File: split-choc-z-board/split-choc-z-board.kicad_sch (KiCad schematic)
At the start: 76 parts, among them J1 USB4105-GF-A, J2 USB4105-GF-A, SW1 SW_SPST, SW10 SW_SPST, SW11 SW_SPST, SW12 SW_SPST, SW13 SW_SPST, SW14 SW_SPST, SW15 SW_SPST, SW16 SW_SPST, SW17 SW_SPST, SW18 SW_SPST, SW19 SW_SPST, SW2 SW_SPST, SW20 SW_SPST, SW21 SW_SPST, SW22 SW_SPST, SW3 SW_SPST, SW4 SW_SPST, SW5 SW_SPST, SW6 SW_SPST, SW7 SW_SPST, SW8 SW_SPST, SW9 SW_SPST, U1 USBLC6-2SC6, U2 RP2040, U3 NCP1117-3.3_SOT223, U4 W25Q128JVS, U5 USBLC6-2SC6, X1 ABM8-272-T3

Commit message: Placed all components properly! 😄
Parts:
- removed H1, H2: MountingHole_Pad_MP, TestPoint:TestPoint_Pad_2.0x2.0mm, symbol Mechanical:MountingHole_Pad_MP
- removed U1: USBLC6-2SC6, Package_TO_SOT_SMD:SOT-23-6, symbol Power_Protection:USBLC6-2SC6
- added C17: 100n, Capacitor_SMD:C_0402_1005Metric, symbol Device:C
- added D_CLK1, D_DATA1, GND1, GP24, GP25: TestPoint, TestPoint:TestPoint_Pad_D2.0mm, symbol Connector:TestPoint
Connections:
- net +3.3V is gone; now on net +3V3: C10.1, C11.1, C5.1, C6.1, C7.1, C8.1, C9.1
- net +3V3: no longer SW1.2 (B), SW10.2 (B), SW11.2 (B), SW12.2 (B), SW13.2 (B), SW14.2 (B), SW15.2 (B), SW16.2 (B), SW17.2 (B), SW18.2 (B), SW19.2 (B), SW2.2 (B), SW20.2 (B), SW3.2 (B), SW4.2 (B), SW5.2 (B), SW6.2 (B), SW7.2 (B), SW8.2 (B), SW9.2 (B), U2.3 (GPIO1), U2.4 (GPIO2), U2.5 (GPIO3), U2.6 (GPIO4)
- net B-B_D+: now also U5.1 (I/O1), U5.6 (I/O1)
- net B-B_D-: now also U5.3 (I/O2), U5.4 (I/O2)
- net DEBUG_CLK: now also D_CLK1.1
- net DEBUG_DATA: now also D_DATA1.1
- net GND: now also C17.1, GND1.1
- net RST: now also C17.2
- net USB_D+: no longer U5.1 (I/O1), U5.6 (I/O1)
- net USB_D-: no longer U5.3 (I/O2), U5.4 (I/O2)
- net GP24: now reaches U2.36 (GPIO24)
- net GP24: now also GP24.1
- net GP25: now reaches U2.37 (GPIO25)
- net GP25: now also GP25.1
- new net Col_1: SW1.2 (B), SW13.2 (B), SW17.2 (B), SW5.2 (B), SW9.2 (B), U2.3 (GPIO1)
- new net Col_2: SW10.2 (B), SW14.2 (B), SW18.2 (B), SW2.2 (B), SW6.2 (B), U2.4 (GPIO2)
- new net Col_3: SW11.2 (B), SW15.2 (B), SW19.2 (B), SW3.2 (B), SW7.2 (B), U2.5 (GPIO3)
- new net Col_4: SW12.2 (B), SW16.2 (B), SW20.2 (B), SW4.2 (B), SW8.2 (B), U2.6 (GPIO4)
- no-connect marks 24 -> 22
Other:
- note removed: "ESD Protection"
- moved on the sheet: R8, SW22

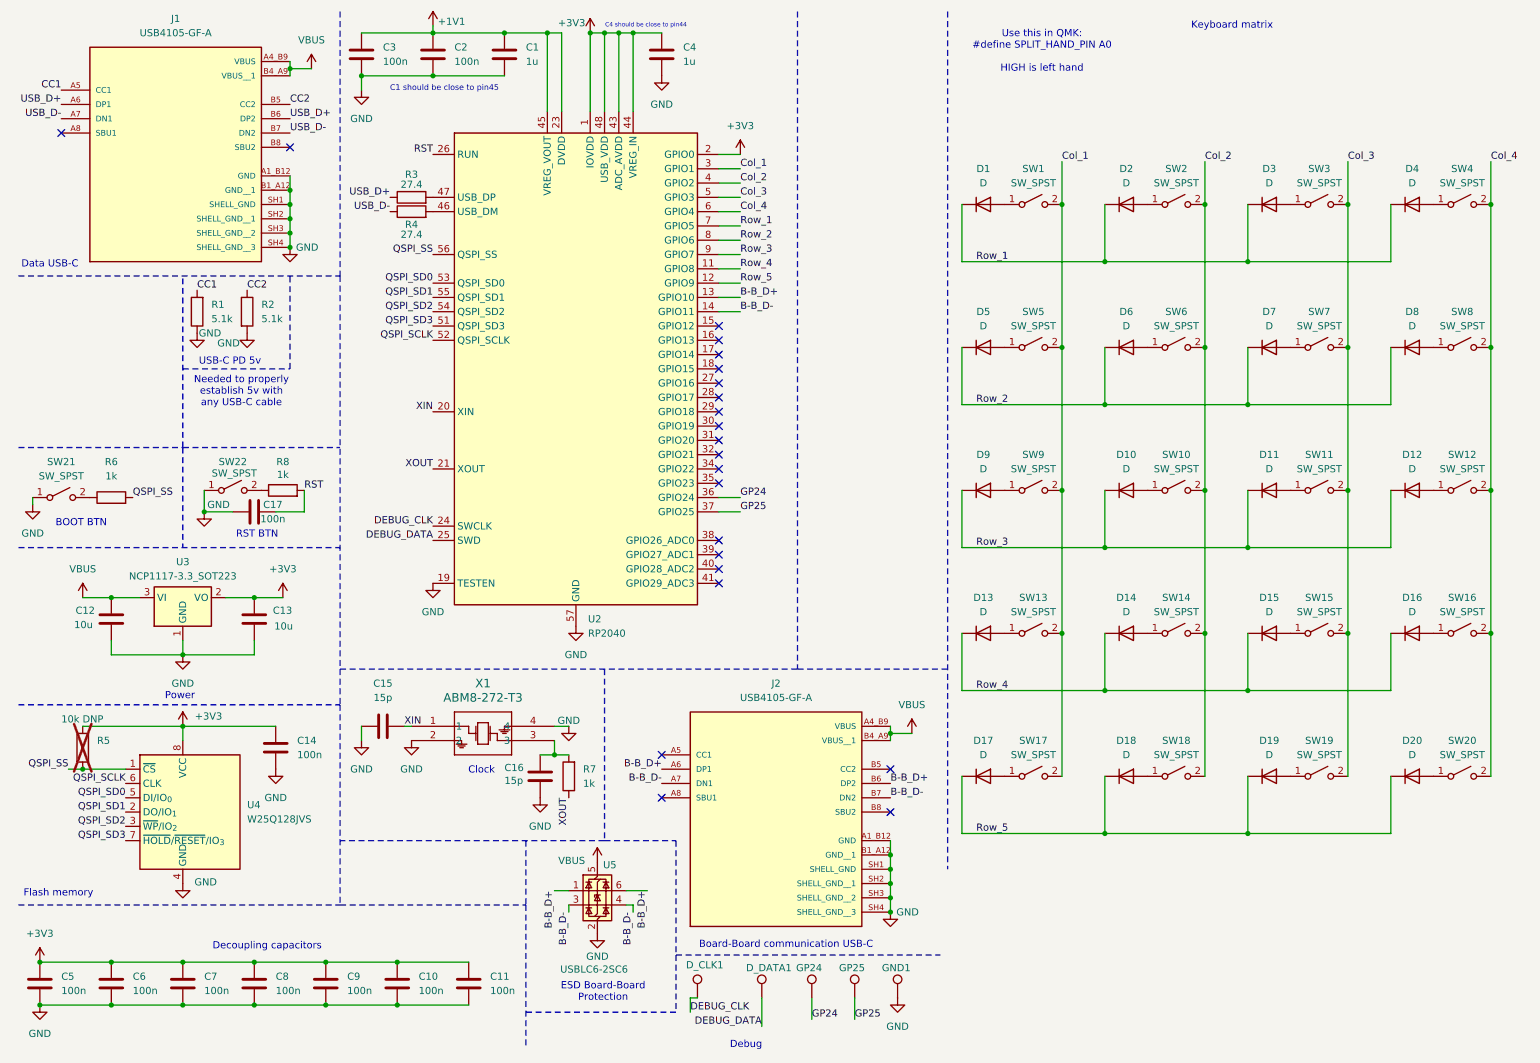
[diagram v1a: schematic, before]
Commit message: Routed left side
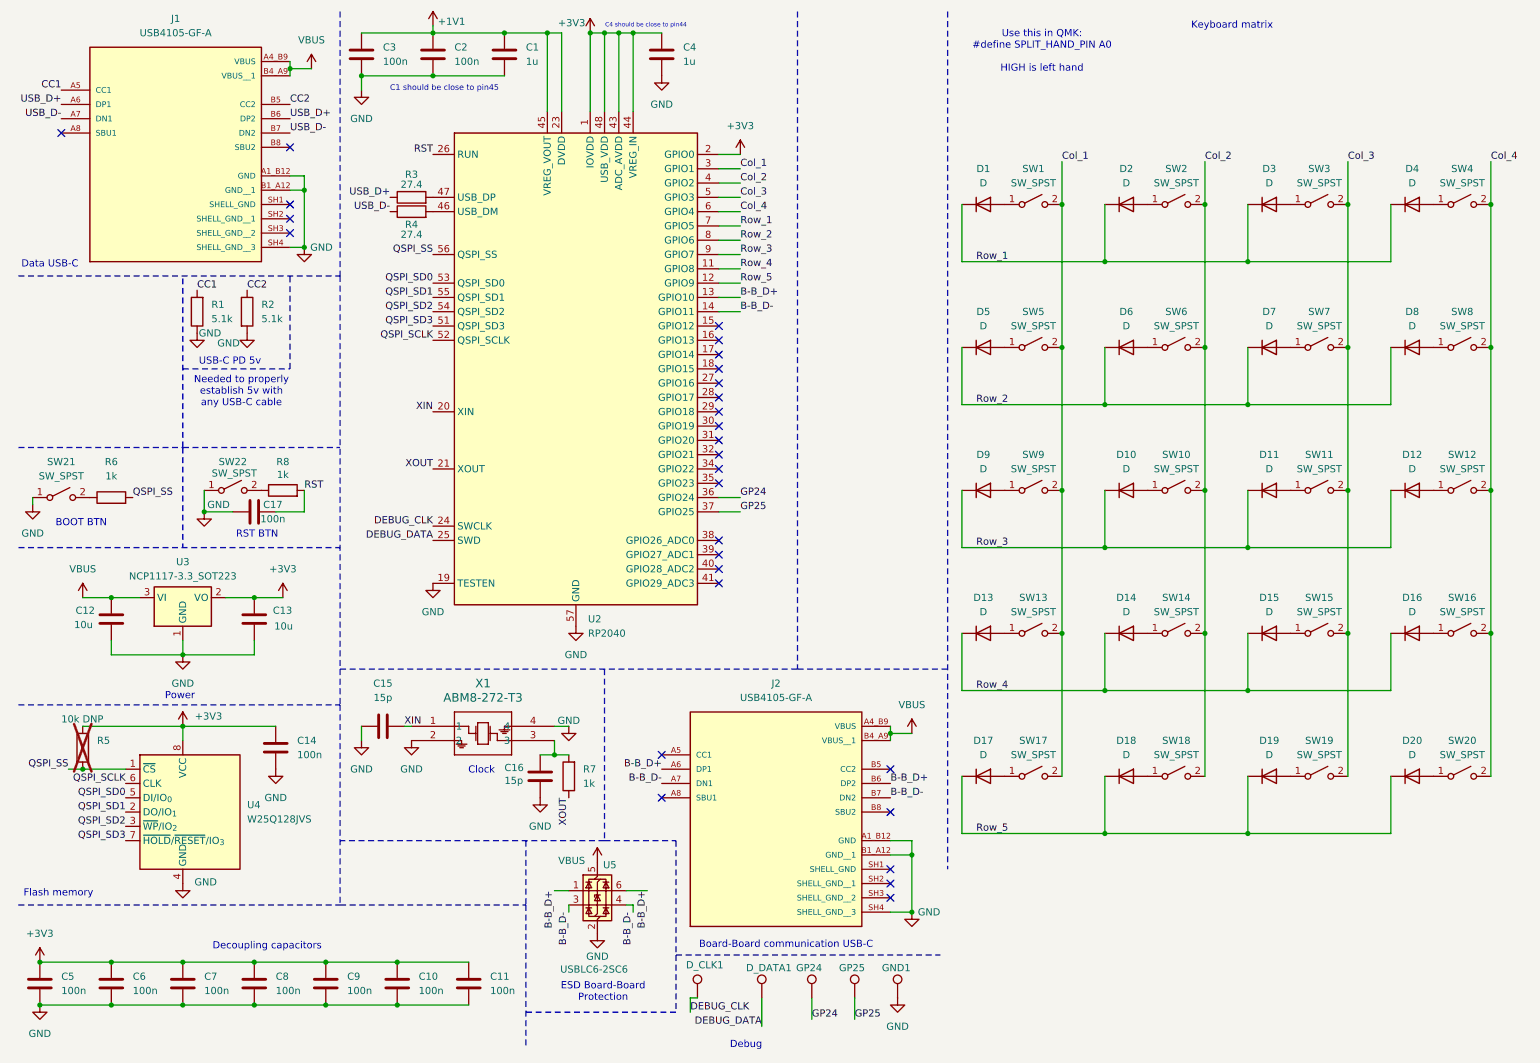
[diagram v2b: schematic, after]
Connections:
- net GND: no longer J1.SH1 (SHELL_GND), J1.SH2 (SHELL_GND__1), J1.SH3 (SHELL_GND__2), J2.SH1 (SHELL_GND), J2.SH2 (SHELL_GND__1), J2.SH3 (SHELL_GND__2)
- no-connect marks 22 -> 28
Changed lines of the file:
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@@
 	)
 	(junction
-		(at 167.64 162.56)
+		(at 171.45 162.56)
 		(diameter 0)
 		(color 0 0 0 0)
@@
 	)
 	(junction
-		(at 60.96 46.99)
-		(diameter 0)
-		(color 0 0 0 0)
-	)
-	(junction
 		(at 231.14 133.35)
 		(diameter 0)
@@
 	)
 	(junction
-		(at 167.64 167.64)
-		(diameter 0)
-		(color 0 0 0 0)
-	)
-	(junction
 		(at 119.38 16.51)
 		(diameter 0)
@@
 	)
 	(junction
-		(at 60.96 44.45)
+		(at 63.5 44.45)
 		(diameter 0)
 		(color 0 0 0 0)
@@
 	)
 	(junction
-		(at 167.64 172.72)
+		(at 99.06 16.51)
 		(diameter 0)
 		(color 0 0 0 0)
 	)
 	(junction
-		(at 99.06 16.51)
+		(at 63.5 54.61)
 		(diameter 0)
 		(color 0 0 0 0)
@@
 	)
 	(junction
-		(at 60.96 49.53)
-		(diameter 0)
-		(color 0 0 0 0)
-	)
-	(junction
 		(at 80.01 181.61)
 		(diameter 0)
@@
 	)
 	(junction
-		(at 60.96 52.07)
-		(diameter 0)
-		(color 0 0 0 0)
-	)
-	(junction
 		(at 223.52 72.39)
 		(diameter 0)
@@
 	)
 	(junction
-		(at 198.12 97.79)
+		(at 171.45 172.72)
 		(diameter 0)
 		(color 0 0 0 0)
 	)
 	(junction
-		(at 167.64 165.1)
+		(at 198.12 97.79)
 		(diameter 0)
 		(color 0 0 0 0)
@@
 	)
 	(junction
-		(at 167.64 170.18)
-		(diameter 0)
-		(color 0 0 0 0)
-	)
-	(junction
 		(at 198.12 72.39)
 		(diameter 0)
@@
 	)
 	(junction
-		(at 60.96 54.61)
-		(diameter 0)
-		(color 0 0 0 0)
-	)
-	(junction
 		(at 205.74 57.15)
 		(diameter 0)
@@
 	)
 	(no_connect
+		(at 60.96 49.53)
+	)
+	(no_connect
+		(at 60.96 46.99)
+	)
+	(no_connect
 		(at 137.16 111.76)
 	)
@@
 	)
 	(no_connect
+		(at 167.64 165.1)
+	)
+	(no_connect
 		(at 137.16 106.68)
 	)
@@
 	)
 	(no_connect
+		(at 167.64 167.64)
+	)
+	(no_connect
 		(at 127 152.4)
 	)
@@
 	)
 	(no_connect
+		(at 167.64 170.18)
+	)
+	(no_connect
 		(at 137.16 83.82)
 	)
@@
 	)
 	(no_connect
+		(at 60.96 52.07)
+	)
+	(no_connect
 		(at 137.16 91.44)
 	)
@@
 	(wire
 		(pts
-			(xy 60.96 46.99) (xy 60.96 49.53)
-		)
-		(stroke
-			(width 0)
-			(type default)
-		)
-	)
-	(wire
-		(pts
-			(xy 167.64 167.64) (xy 167.64 170.18)
-		)
-		(stroke
-			(width 0)
-			(type default)
-		)
-	)
-	(wire
-		(pts
 			(xy 180.34 158.75) (xy 180.34 148.59)
 		)
@@
 	(wire
 		(pts
-			(xy 167.64 162.56) (xy 167.64 165.1)
+			(xy 171.45 162.56) (xy 171.45 172.72)
 		)
 		(stroke
@@
 	(wire
 		(pts
-			(xy 29.21 189.23) (xy 41.91 189.23)
+			(xy 63.5 41.91) (xy 60.96 41.91)
 		)
 		(stroke
@@
 	(wire
 		(pts
-			(xy 81.28 139.7) (xy 82.55 139.7)
+			(xy 29.21 189.23) (xy 41.91 189.23)
 		)
 		(stroke
@@
 	(wire
 		(pts
-			(xy 49.53 116.84) (xy 54.61 116.84)
+			(xy 81.28 139.7) (xy 82.55 139.7)
 		)
 		(stroke
@@
 	(wire
 		(pts
-			(xy 167.64 140.97) (xy 171.45 140.97)
+			(xy 49.53 116.84) (xy 54.61 116.84)
 		)
 		(stroke
@@
 	(wire
 		(pts
-			(xy 167.64 165.1) (xy 167.64 167.64)
+			(xy 167.64 140.97) (xy 171.45 140.97)
 		)
 		(stroke
@@
 	(wire
 		(pts
-			(xy 60.96 44.45) (xy 60.96 46.99)
+			(xy 223.52 39.37) (xy 223.52 46.99)
 		)
 		(stroke
@@
 	(wire
 		(pts
-			(xy 223.52 39.37) (xy 223.52 46.99)
+			(xy 171.45 162.56) (xy 167.64 162.56)
 		)
 		(stroke
@@
 	(wire
 		(pts
-			(xy 60.96 52.07) (xy 60.96 54.61)
+			(xy 63.5 44.45) (xy 63.5 54.61)
 		)
 		(stroke
@@
 	(wire
 		(pts
+			(xy 167.64 172.72) (xy 171.45 172.72)
+		)
+		(stroke
+			(width 0)
+			(type default)
+		)
+	)
+	(wire
+		(pts
 			(xy 73.66 139.7) (xy 73.66 142.24)
 		)
@@
 	(wire
 		(pts
-			(xy 167.64 170.18) (xy 167.64 172.72)
-		)
-		(stroke
-			(width 0)
-			(type default)
-		)
-	)
-	(wire
-		(pts
 			(xy 161.29 191.77) (xy 161.29 187.96)
 		)
@@
 	(wire
 		(pts
+			(xy 60.96 54.61) (xy 63.5 54.61)
+		)
+		(stroke
+			(width 0)
+			(type default)
+		)
+	)
+	(wire
+		(pts
 			(xy 248.92 97.79) (xy 248.92 123.19)
 		)
@@
 	(wire
 		(pts
+			(xy 171.45 160.02) (xy 167.64 160.02)
+		)
+		(stroke
+			(width 0)
+			(type default)
+		)
+	)
+	(wire
+		(pts
 			(xy 274.32 46.99) (xy 274.32 72.39)
 		)
@@
 	(wire
 		(pts
-			(xy 60.96 41.91) (xy 60.96 44.45)
+			(xy 63.5 41.91) (xy 63.5 44.45)
 		)
 		(stroke
@@
 		)
 	)
-	(polyline
+	(wire
 		(pts
-			(xy 69.85 59.69) (xy 69.85 129.54)
+			(xy 63.5 44.45) (xy 60.96 44.45)
 		)
 		(stroke
 			(width 0)
-			(type dash)
+			(type default)
 		)
 	)
-	(wire
+	(polyline
 		(pts
-			(xy 60.96 49.53) (xy 60.96 52.07)
+			(xy 69.85 59.69) (xy 69.85 129.54)
 		)
 		(stroke
 			(width 0)
-			(type default)
+			(type dash)
 		)
 	)
@@
 	(wire
 		(pts
-			(xy 167.64 160.02) (xy 167.64 162.56)
+			(xy 171.45 160.02) (xy 171.45 162.56)
 		)
 		(stroke
@@
 	(symbol
 		(lib_id "power:GND")
-		(at 60.96 54.61 0)
+		(at 63.5 54.61 0)
 		(unit 1)
 		(exclude_from_sim no)
@@
 		(dnp no)
 		(property "Reference" "#PWR021"
-			(at 60.96 60.96 0)
+			(at 63.5 60.96 0)
 			(effects
 				(font
@@
 		)
 		(property "Value" "GND"
-			(at 64.008 54.61 0)
+			(at 66.548 54.61 0)
 			(effects
 				(font
@@
 		)
 		(property "Footprint" ""
-			(at 60.96 54.61 0)
+			(at 63.5 54.61 0)
 			(effects
 				(font
@@
 		)
 		(property "Datasheet" ""
-			(at 60.96 54.61 0)
+			(at 63.5 54.61 0)
 			(effects
 				(font
@@
 		)
 		(property "Description" "Power symbol creates a global label with name \"GND\" , ground"
-			(at 60.96 54.61 0)
+			(at 63.5 54.61 0)
 			(effects
 				(font
@@
 	(symbol
 		(lib_id "power:GND")
-		(at 167.64 172.72 0)
+		(at 171.45 172.72 0)
 		(unit 1)
 		(exclude_from_sim no)
@@
 		(dnp no)
 		(property "Reference" "#PWR031"
-			(at 167.64 179.07 0)
+			(at 171.45 179.07 0)
 			(effects
 				(font
@@
 		)
 		(property "Value" "GND"
-			(at 170.688 172.72 0)
+			(at 174.498 172.72 0)
 			(effects
 				(font
@@
 		)
 		(property "Footprint" ""
-			(at 167.64 172.72 0)
+			(at 171.45 172.72 0)
 			(effects
 				(font
@@
 		)
 		(property "Datasheet" ""
-			(at 167.64 172.72 0)
+			(at 171.45 172.72 0)
 			(effects
 				(font
@@
 		)
 		(property "Description" "Power symbol creates a global label with name \"GND\" , ground"
-			(at 167.64 172.72 0)
+			(at 171.45 172.72 0)
 			(effects
 				(font

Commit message: Finished routing USB and added easier to use debug connectors
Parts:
- removed D_CLK1, D_DATA1: TestPoint, TestPoint:TestPoint_Pad_D2.0mm, symbol Connector:TestPoint
- added J3: Conn_01x04_Pin, Connector_PinHeader_2.54mm:PinHeader_1x04_P2.54mm_Vertical, symbol Connector:Conn_01x04_Pin
- added J4: Conn_01x02, Connector_PinHeader_2.54mm:PinHeader_1x02_P2.54mm_Vertical, symbol Connector_Generic:Conn_01x02
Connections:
- net +3V3: now also J3.2 (Pin_2)
- net DEBUG_CLK: now also J3.4 (Pin_4)
- net DEBUG_DATA: now also J3.3 (Pin_3)
- net GND: now also J3.1 (Pin_1), J4.1 (Pin_1)
- net GP24: now also J4.2 (Pin_2)
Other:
- note added: "Debug pins"
